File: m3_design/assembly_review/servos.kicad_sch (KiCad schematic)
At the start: 12 parts, among them J122 SERVO 3x4

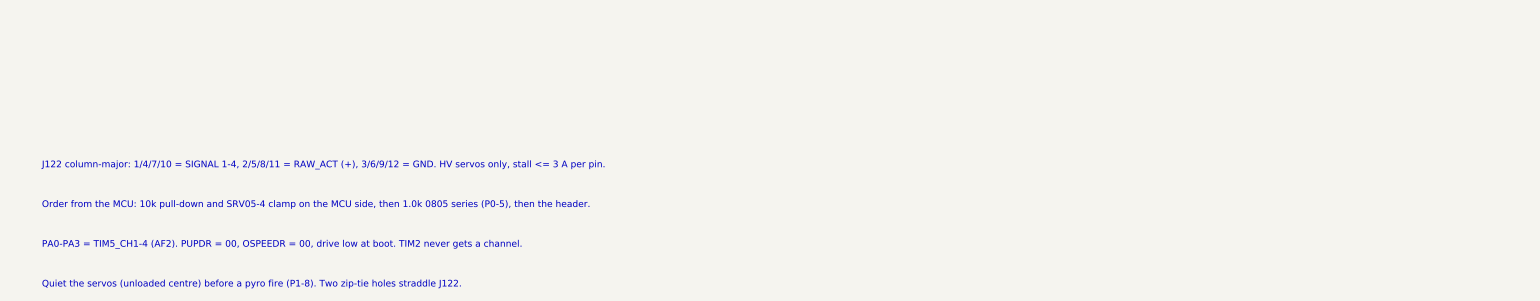
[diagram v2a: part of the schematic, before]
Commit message: M3-ASSY-R4: R3 validation fixes, new IMU, fault-tolerant pyro sensing
The board, schematic sheets and footprint library are generated from
R3 (533af8e) by m3_design/r4_build.sh (r4_lib.py, r4_sch.py,
r4_pcb.py). docs/REQUIREMENTS.md states what the board must do;
docs/M3_R4.md records every change, the thirteen evaluation passes
(twelve independent reviews) and the accepted deviations.

- IMU: ST LSM6DSV320X (16 g and 320 g, 4000 dps)
- Pyro: black ARM and orange igniter terminals, eight pyro spacing
  rules in m3.kicad_dru, sense dividers of 2 x 5.1k over 2 x 2k in
  parallel, 4.7k at each ADC pin (R168-R172)
- Pull-pin on a JST PH connector; JLC tooling holes
- Fab: Standard PCBA, 84 BOM lines, 205 placed parts, $80.12 per board
  at five boards (tools/jlc_cost.py); placement rotations verified
- Gate: tools/check.sh DRC 0, unconnected 0, schematic parity 0, ERC 0,
  audit OK; m3_design/check_actuators.py OK

Nothing has been built or measured, and there is no R4 firmware. The
open owner decisions and the bench tests are listed in STATUS.md.

Co-Authored-By: Claude Opus 5.5 <noreply@anthropic.com>
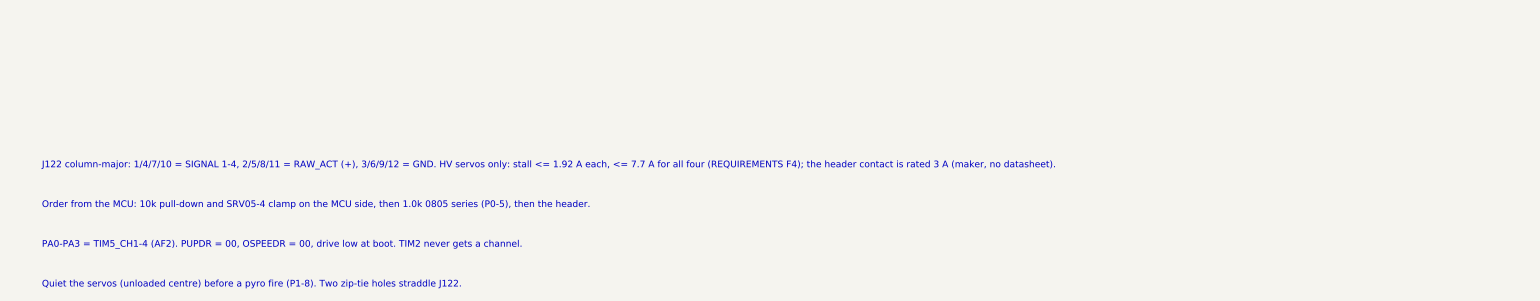
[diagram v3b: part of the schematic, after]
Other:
- note added: "J122 column-major: 1/4/7/10 = SIGNAL 1-4, 2/5/8/11 = RAW_ACT (+), 3/6/9/12 = GND. HV servos only: stall <= 1.92 A each, <= 7.7 A for all four (REQUIREMENTS F4); the header contact is rated 3 A (maker, no datasheet)."
- note removed: "J122 column-major: 1/4/7/10 = SIGNAL 1-4, 2/5/8/11 = RAW_ACT (+), 3/6/9/12 = GND. HV servos only, stall <= 3 A per pin."
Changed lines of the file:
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@@
 		(title "13 | Servo outputs")
 		(date "2026-09-25")
-		(rev "M3-ASSY-R3")
+		(rev "M3-ASSY-R4")
 		(company "Single-board M3 candidate; actuator merge, not bench-verified"))
 	(symbol
@@
 			(justify left))
 )
-	(text "J122 column-major: 1/4/7/10 = SIGNAL 1-4, 2/5/8/11 = RAW_ACT (+), 3/6/9/12 = GND. HV servos only, stall <= 3 A per pin."
+	(text "J122 column-major: 1/4/7/10 = SIGNAL 1-4, 2/5/8/11 = RAW_ACT (+), 3/6/9/12 = GND. HV servos only: stall <= 1.92 A each, <= 7.7 A for all four (REQUIREMENTS F4); the header contact is rated 3 A (maker, no datasheet)."
 		(at 20.32 245 0)
 		(effects
